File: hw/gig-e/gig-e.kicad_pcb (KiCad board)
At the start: 4 copper layers, 149 x 111.1 mm, 181 parts, among them U201 FDT434P, U202 KSZ9021GQ, U203 MIC5207-2.5YM5, U301 FDT434P, U302 KSZ9021GQ, U303 MIC5207-2.5YM5, X201 25MHz, X301 25MHz

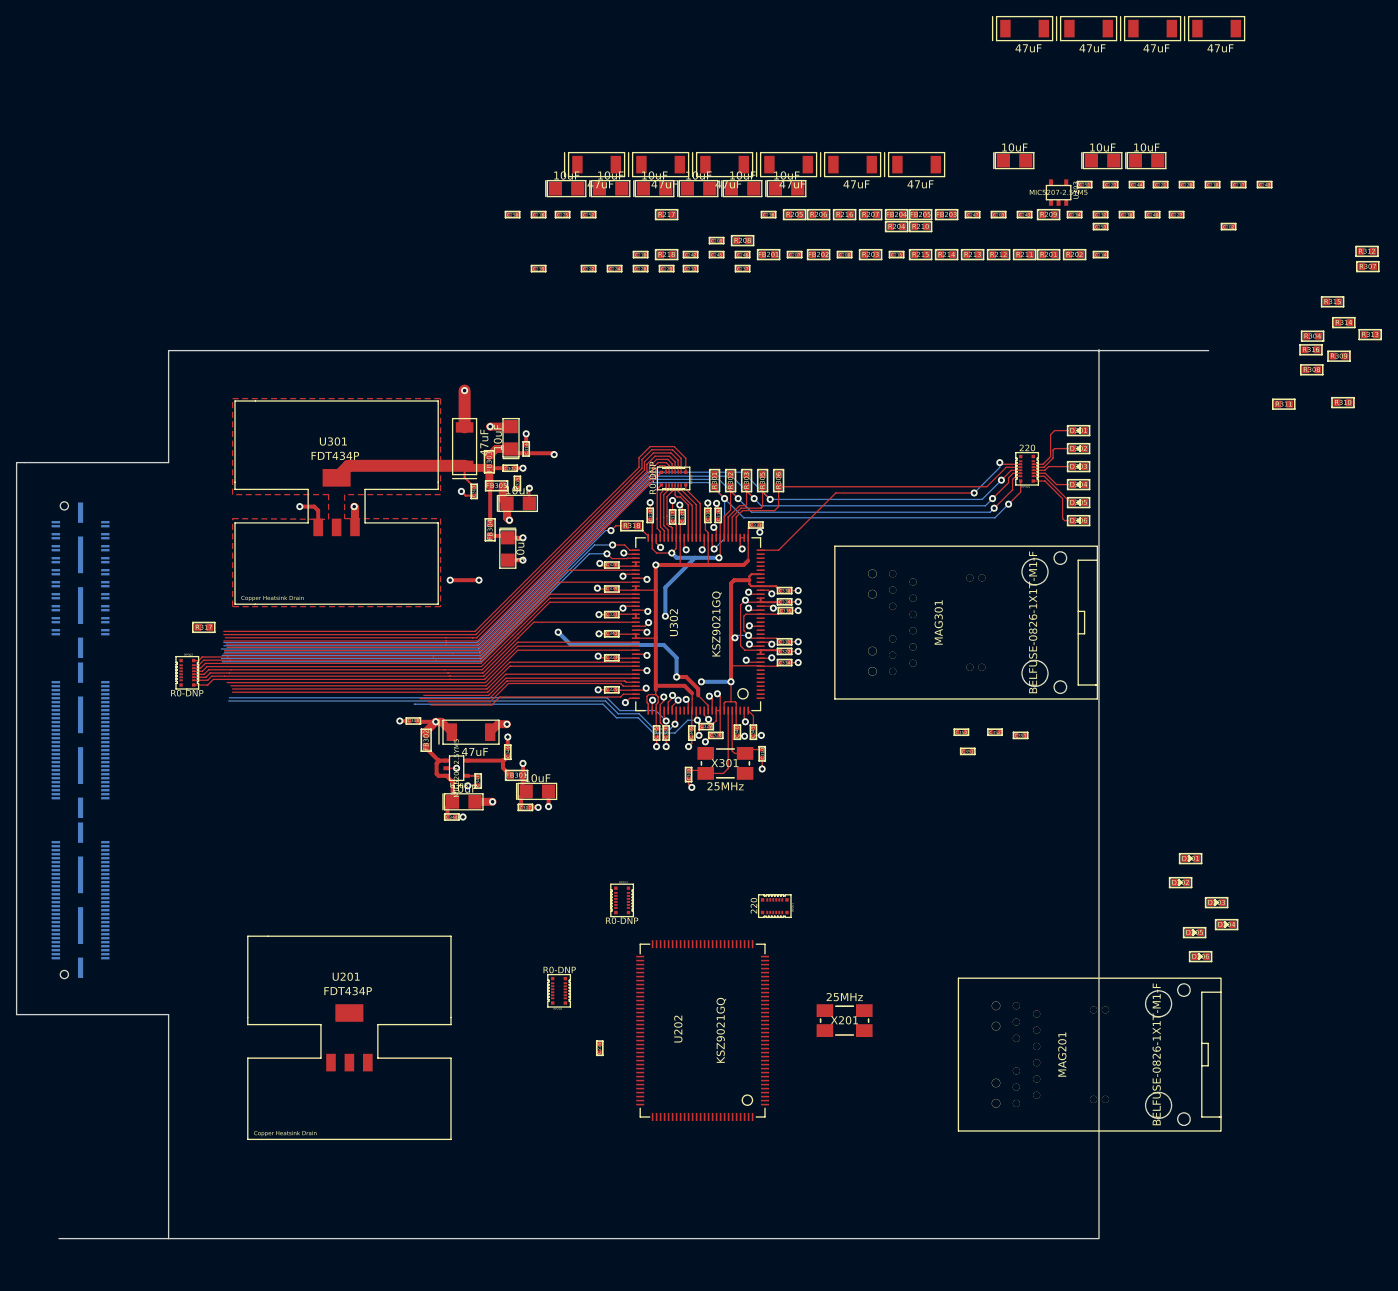
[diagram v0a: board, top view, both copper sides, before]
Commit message: gig-e board for DE2-115 completed
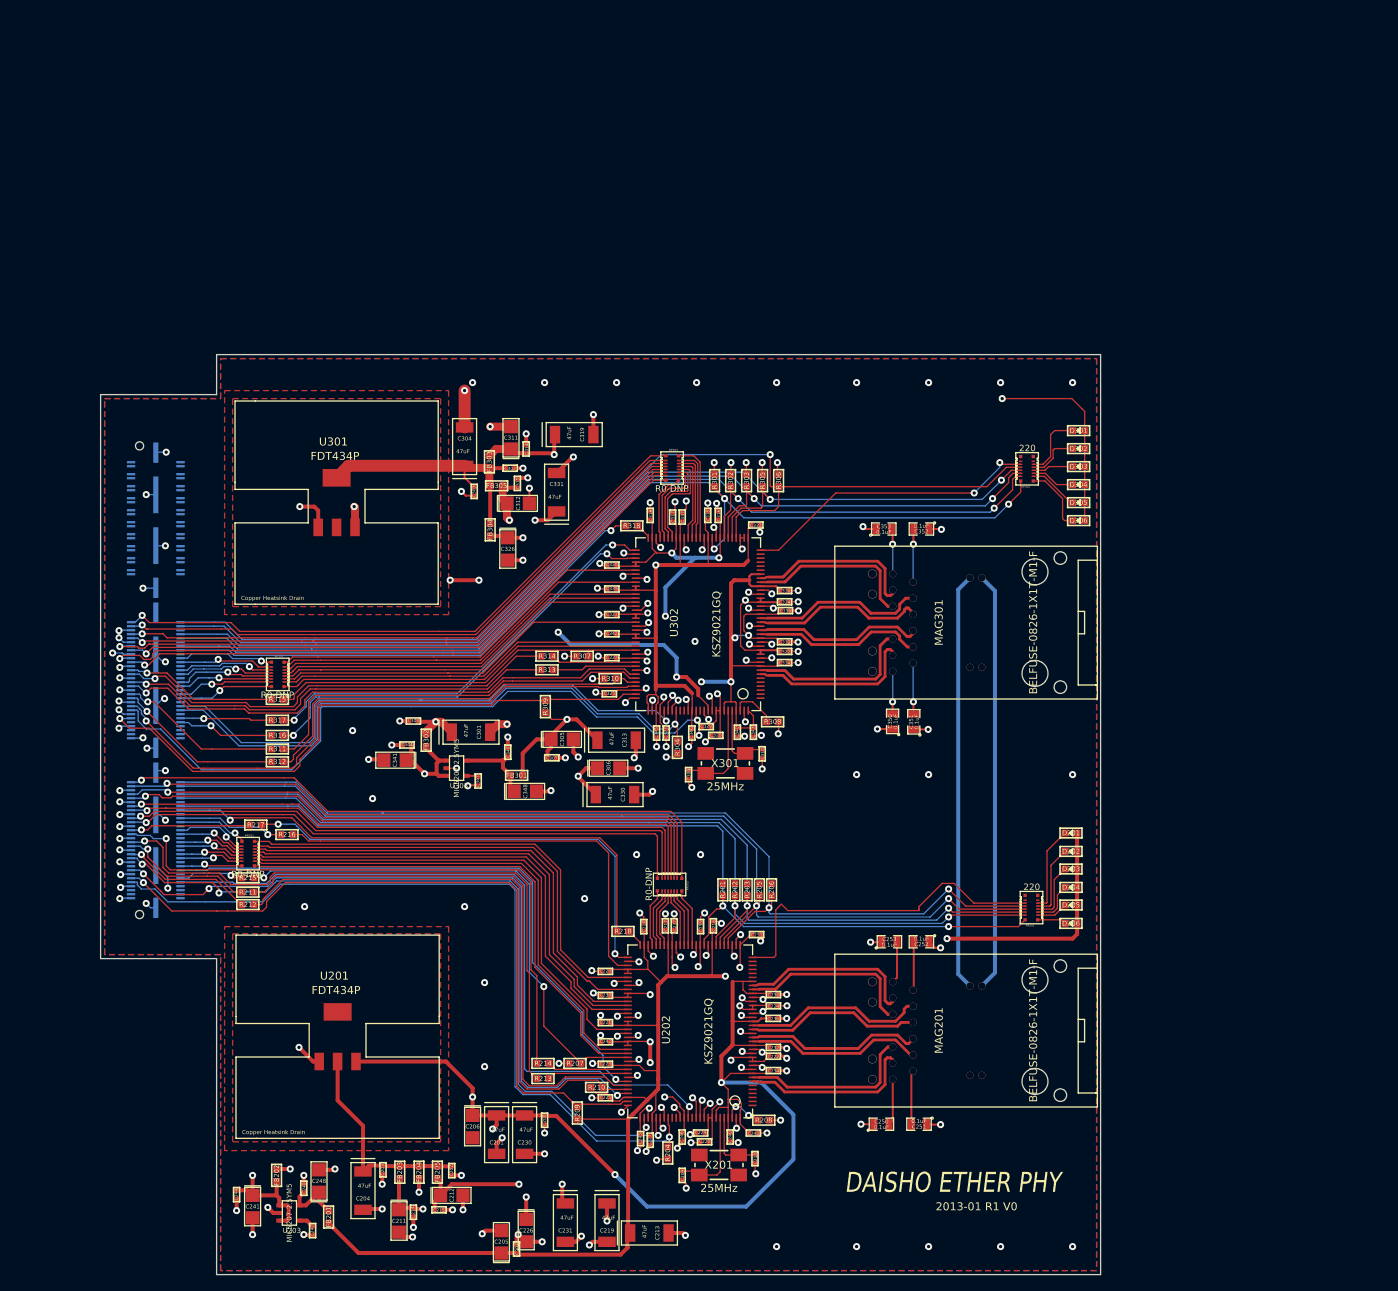
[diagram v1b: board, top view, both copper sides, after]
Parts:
- C250, C251, C252, C253, C350, C351, C352, C353: footprint GSG-0402 -> SM0805
- moved C249 173.7 mm to (114.9, 162.7), turned to 90 degrees
- moved C244 169.1 mm to (106.5, 163.5), turned to 270 degrees
- moved C213 166.4 mm to (158.1, 168.3)
- moved U203 159.7 mm to (113.1, 165.8), turned to 270 degrees
- moved C230 159.0 mm to (142.5, 156.0), turned to 270 degrees
- moved C212 155.8 mm to (133.4, 163.6)
- moved C202 152.8 mm to (133.4, 160.5), turned to 270 degrees
- moved C247 151.4 mm to (116.0, 168.0), turned to 270 degrees
- moved R312 150.4 mm to (111.6, 109.4), turned to 180 degrees
- moved C214 147.3 mm to (128.6, 165.7), turned to 270 degrees
- moved C204 142.1 mm to (122.3, 163.0), turned to 270 degrees
- moved C203 142.0 mm to (124.8, 160.4), turned to 270 degrees
- moved R315 141.0 mm to (111.6, 101.6), turned to 180 degrees
- moved R316 137.9 mm to (111.6, 106.1), turned to 180 degrees
- moved C211 137.8 mm to (126.8, 166.8), turned to 270 degrees
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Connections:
- JP101 pad 101: PHY0_GM_TXD7 -> PHY0_GM_TXD0
- JP101 pad 102: PHY1_GM_TXD7 -> PHY0_PHYADDR4
- JP101 pad 103: PHY0_GM_TXD6 -> PHY0_GM_TXD1
- JP101 pad 104: PHY1_GM_TXD6 -> PHY0_PHYADDR3
- JP101 pad 107: PHY0_GM_TXD5 -> PHY0_GM_TXD2
- JP101 pad 108: PHY1_GM_TXD5 -> PHY0_PHYADDR2
- JP101 pad 109: PHY0_GM_TXD4 -> PHY0_GM_TXD3
- JP101 pad 110: PHY1_GM_TXD4 -> PHY0_PHYADDR1
- JP101 pad 113: PHY0_GM_TXD3 -> PHY0_GM_TXD4
- JP101 pad 114: PHY1_GM_TXD3 -> PHY0_PHYADDR0
- JP101 pad 115: PHY0_GM_TXD2 -> PHY0_GM_TXD5
- JP101 pad 116: PHY1_GM_TXD2 -> PHY0_GM_TX_ER
- JP101 pad 119: PHY0_GM_TXD1 -> PHY0_GM_TXD6
- JP101 pad 120: PHY1_GM_TXD1 -> PHY0_GM_TX_EN
- JP101 pad 121: PHY0_GM_TXD0 -> PHY0_GM_TXD7
- JP101 pad 122: PHY1_GM_TXD0 -> PHY0_GM_RXD7
- JP101 pad 125: PHY0_PHYADDR1 -> PHY0_GM_GTK_CLK
- JP101 pad 126: PHY1_PHYADDR1 -> PHY0_GM_RXD6
- JP101 pad 127: PHY0_PHYADDR2 -> PHY0_GM_RX_ERR
- JP101 pad 128: PHY1_PHYADDR2 -> PHY0_GM_RXD5
- JP101 pad 131: PHY0_PHYADDR3 -> PHY0_GM_RX_CLK
- JP101 pad 132: PHY1_PHYADDR3 -> PHY0_GM_RXD4
- JP101 pad 133: PHY0_PHYADDR4 -> PHY0_GM_MDC
- JP101 pad 134: PHY1_PHYADDR4 -> PHY0_GM_RXD3
- JP101 pad 137: PHY0_RXDV -> PHY0_GM_MIO
- JP101 pad 138: PHY1_RXDV -> PHY0_GM_RXD2
- JP101 pad 139: PHY0_TX_CLK -> PHY0_CLK125_NDO
- JP101 pad 140: PHY1_TX_CLK -> PHY0_GM_RXD1
- JP101 pad 143: PHY0_HW_RST -> (no net)
- JP101 pad 144: PHY1_HW_RST -> PHY0_GM_RXD0
- JP101 pad 146: PHY1_COL -> PHY0_CRS
- JP101 pad 149: PHY1_CRS -> PHY0_INT_N
- JP101 pad 150: PHY1_CRS -> PHY0_GM_RXDV
- JP101 pad 151: (no net) -> PHY0_HW_RST
- JP101 pad 152: (no net) -> PHY0_TX_CLK
- JP101 pad 41: PHY0_GM_MDC -> PHY1_GM_TXD0
- JP101 pad 42: PHY1_GM_MDC -> PHY1_PHYADDR4
- JP101 pad 43: PHY0_GM_MIO -> PHY1_GM_TXD1
- JP101 pad 44: PHY1_GM_MIO -> PHY1_PHYADDR3
- JP101 pad 47: PHY0_GM_RX_CLK -> PHY1_GM_TXD2
- JP101 pad 48: PHY1_GM_RX_CLK -> PHY1_PHYADDR2
- JP101 pad 49: PHY0_GM_RX_ERR -> PHY1_GM_TXD3
- JP101 pad 50: PHY1_GM_RX_ERR -> PHY1_PHYADDR1
- JP101 pad 53: PHY0_GM_RXDV -> PHY1_GM_TXD4
- JP101 pad 54: PHY1_GM_RXDV -> PHY1_PHYADDR0
- JP101 pad 55: PHY0_GM_RXD7 -> PHY1_GM_TXD5
- JP101 pad 56: PHY1_GM_RXD7 -> PHY1_GM_TX_ER
- JP101 pad 59: PHY0_GM_RXD6 -> PHY1_GM_TXD6
- JP101 pad 60: PHY1_GM_RXD6 -> PHY1_GM_RXD7
- JP101 pad 61: PHY0_GM_RXD5 -> PHY1_GM_TXD7
- JP101 pad 62: PHY1_GM_RXD5 -> PHY1_GM_RXD6
- JP101 pad 65: PHY0_GM_RXD4 -> PHY1_GM_RXDV
- JP101 pad 66: PHY1_GM_RXD4 -> PHY1_GM_RXD5
- JP101 pad 67: PHY0_GM_RXD3 -> PHY1_GM_RX_ERR
- JP101 pad 68: PHY1_GM_RXD3 -> PHY1_GM_RXD4
- JP101 pad 71: PHY0_GM_RXD2 -> PHY1_GM_RX_CLK
- JP101 pad 72: PHY1_GM_RXD2 -> PHY1_GM_RXD3
- JP101 pad 73: PHY0_GM_RXD1 -> PHY1_CRS
- JP101 pad 74: PHY1_GM_RXD1 -> PHY1_GM_RXD2
- JP101 pad 77: PHY0_GM_RXD0 -> PHY1_GM_MDC
- JP101 pad 78: PHY1_GM_RXD0 -> PHY1_GM_RXD1
- JP101 pad 79: PHY0_GM_TX_EN -> PHY1_GM_MIO
- JP101 pad 80: PHY1_GM_TX_EN -> PHY1_GM_RXD0
- JP101 pad 83: PHY0_GM_GTK_CLK -> PHY1_COL
- JP101 pad 84: PHY1_GM_GTK_CLK -> PHY1_CLK125_NDO
- JP101 pad 85: PHY0_GM_TX_ER -> PHY1_TX_CLK
- JP101 pad 86: PHY1_GM_TX_ER -> PHY1_HW_RST
- JP101 pad 89: PHY0_CLK125_NDO -> PHY1_INT_N
- JP101 pad 90: PHY1_CLK125_NDO -> PHY1_GM_GTK_CLK
- JP101 pad 91: PHY0_PHYADDR0 -> (no net)
- JP101 pad 92: PHY1_PHYADDR0 -> PHY1_GM_TX_EN
- MAG201 pad 4: PHY0_TXRXP_B -> PHY0_TXRXM_B
- MAG201 pad 5: PHY0_TXRXM_B -> PHY0_TXRXP_B
- MAG201 pad 8: PHY0_TXRXP_D -> PHY0_TXRXM_D
- MAG201 pad 9: PHY0_TXRXM_D -> PHY0_TXRXP_D
- MAG301 pad 4: PHY1_TXRXP_B -> PHY1_TXRXM_B
- MAG301 pad 5: PHY1_TXRXM_B -> PHY1_TXRXP_B
- MAG301 pad 8: PHY1_TXRXP_D -> PHY1_TXRXM_D
- MAG301 pad 9: PHY1_TXRXM_D -> PHY1_TXRXP_D
- RP202 pad 1: /GigE Phy0/RXD7 -> /GigE Phy0/RXD0
- RP202 pad 10: PHY0_GM_RXD1 -> PHY0_GM_RXD6
- RP202 pad 11: PHY0_GM_RXD2 -> PHY0_GM_RXD5
- RP202 pad 12: PHY0_GM_RXD3 -> PHY0_GM_RXD4
- RP202 pad 13: PHY0_GM_RXD4 -> PHY0_GM_RXD3
- RP202 pad 14: PHY0_GM_RXD5 -> PHY0_GM_RXD2
- RP202 pad 15: PHY0_GM_RXD6 -> PHY0_GM_RXD1
- RP202 pad 16: PHY0_GM_RXD7 -> PHY0_GM_RXD0
- RP202 pad 2: /GigE Phy0/RXD6 -> /GigE Phy0/RXD1
- RP202 pad 3: /GigE Phy0/RXD5 -> /GigE Phy0/RXD2
- RP202 pad 4: /GigE Phy0/RXD4 -> /GigE Phy0/RXD3
- RP202 pad 5: /GigE Phy0/RXD3 -> /GigE Phy0/RXD4
- RP202 pad 6: /GigE Phy0/RXD2 -> /GigE Phy0/RXD5
- RP202 pad 7: /GigE Phy0/RXD1 -> /GigE Phy0/RXD6
- RP202 pad 8: /GigE Phy0/RXD0 -> /GigE Phy0/RXD7
- RP202 pad 9: PHY0_GM_RXD0 -> PHY0_GM_RXD7
- U202 pad 96: (no net) -> PHY0_CRS
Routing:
- net GND: track 109.2 -> 600.9 mm, vias 74 -> 219
- net /GigE Phy0/DVDDH: track 0.00 -> 200.9 mm, vias 0 -> 2
- net +3.3V: track 12.2 -> 184.2 mm, vias 0 -> 22
- net /GigE Phy0/AVDDH: track 0.00 -> 168.5 mm, vias 0 -> 5
- net PHY0_PHYADDR4: track 0.00 -> 127.9 mm, vias 0 -> 2
- net PHY0_PHYADDR3: track 0.00 -> 126.8 mm, vias 0 -> 2
- net PHY0_PHYADDR2: track 0.00 -> 125.9 mm, vias 0 -> 2
- net PHY0_PHYADDR1: track 0.00 -> 125.3 mm, vias 0 -> 2
- net PHY0_PHYADDR0: track 0.00 -> 125.1 mm, vias 0 -> 2
- net /GigE Phy0/DVDDL: track 0.00 -> 106.2 mm, vias 0 -> 10
- net PHY0_HW_RST: track 0.00 -> 101.1 mm, vias 0 -> 1
- net PHY0_CLK125_NDO: track 0.00 -> 98.5 mm, vias 0 -> 3
- net /GigE Phy1/DVDDH: track 86.3 -> 181.5 mm, vias 6 -> 10
- net /GigE Phy0/AVDDL: track 0.00 -> 94.6 mm, vias 0 -> 4
- net PHY0_INT_N: track 0.00 -> 91.9 mm, vias 0 -> 1
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- added copper zone on F.Cu, net /GigE Phy0/AVDDL_PMOS
- added copper zone on B.Cu, net GND
- added copper zone on F.Cu, net GND
- added copper zone on Inner1.Cu, net GND
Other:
- board size 149 x 111.1 mm -> 125 x 115 mm
- net class Default: via_drill 0.635 -> 0.4064
- rule pad_to_mask_clearance: 0 -> 0.1524
- board text added: "2013-01 R1 V0"
- board text added: "DAISHO ETHER PHY"

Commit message: hardware update including last minute gig-e corrections
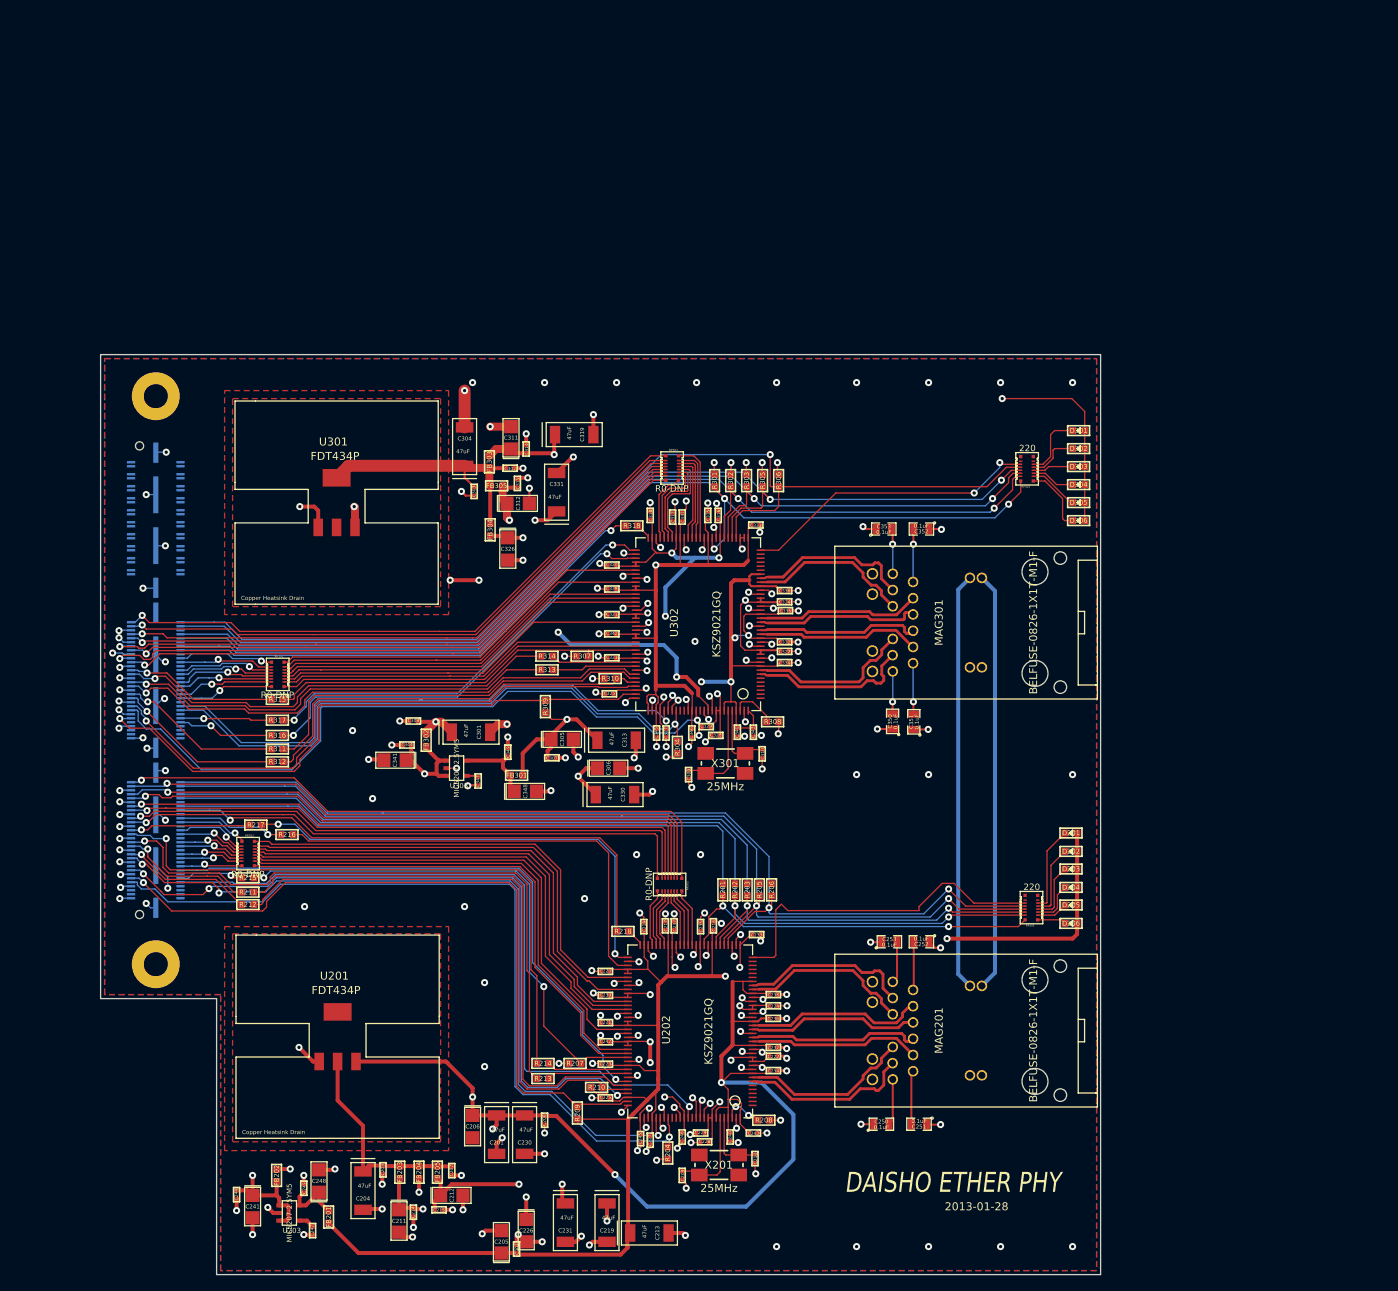
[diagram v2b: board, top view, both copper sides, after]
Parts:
- JP101: footprint TERASIC-HSMC -> TERASIC-HSMC-WITH-MOUNTS
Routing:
- net PHY1_TXRXM_C: track 21.6 -> 20.4 mm
- net PHY1_TXRXP_C: track 21.6 -> 20.4 mm
- net PHY1_TXRXM_D: track 21.5 -> 20.4 mm
- net PHY1_TXRXP_D: track 21.5 -> 20.4 mm
- net PHY0_TXRXM_D: track 22.4 -> 21.4 mm
- net PHY0_TXRXP_D: track 22.4 -> 21.4 mm
- net PHY1_TXRXP_B: track 21.3 -> 20.4 mm
- net PHY1_TXRXM_B: track 21.3 -> 20.5 mm
- net PHY0_TXRXM_A: track 22.2 -> 21.4 mm
- net PHY0_TXRXP_A: track 22.2 -> 21.4 mm
- net PHY1_TXRXM_A: track 21.2 -> 20.4 mm
- net PHY0_TXRXP_B: track 22.2 -> 21.4 mm
- net PHY1_TXRXP_A: track 21.2 -> 20.5 mm
- net PHY0_TXRXM_B: track 22.1 -> 21.5 mm
- net +3.3V: track 184.2 -> 183.5 mm
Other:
- outline, holes or cut-outs redrawn
- board text added: "2013-01-28"
- board text removed: "2013-01 R1 V0"

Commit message: gig-e updates
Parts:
- moved C232 1.00 mm to (174.6, 145.2)
- moved C222 1.00 mm to (174.6, 146.2)
- moved C225 1.00 mm to (151.6, 151.4)
- moved C224 0.86 mm to (174.4, 140.1)
- moved RP201 0.81 mm to (205.1, 127.2)
- moved C234 0.80 mm to (174.4, 148.1)
- moved C238 0.70 mm to (174.3, 138.6)
- moved C328 0.69 mm to (166.8, 106.7), turned to 0 degrees
- moved C329 0.63 mm to (165.4, 105.6)
- moved C327 0.55 mm to (160.2, 106.3)
- moved C316 0.54 mm to (166.5, 78.1)
- moved C335 0.50 mm to (165.3, 78.1)
- moved C242 0.47 mm to (153.0, 144.7)
- moved C336 0.45 mm to (175.6, 90.5)
- moved RP202 0.45 mm to (108.2, 120.5)
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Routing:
- net GND: track 600.9 -> 619.9 mm
- net /GigE Phy0/AVDDH: track 168.2 -> 170.1 mm
- net /GigE Phy0/AVDDL: track 94.6 -> 95.9 mm
- net /GigE Phy1/AVDD_PLL: track 48.9 -> 49.9 mm
- net PHY0_PHYADDR2: track 125.9 -> 124.9 mm
- net PHY0_PHYADDR4: track 127.9 -> 126.9 mm
- net PHY1_CLK125_NDO: track 71.6 -> 72.6 mm
- net /GigE Phy0/LED6: track 43.2 -> 42.3 mm
- net PHY0_PHYADDR1: track 125.3 -> 124.4 mm
- net /GigE Phy0/LED1_D: track 3.59 -> 4.42 mm
- net PHY0_INT_N: track 91.9 -> 92.7 mm
- net /GigE Phy1/DVDDL: track 102.6 -> 103.4 mm
- net /GigE Phy0/LED2_D: track 3.92 -> 4.66 mm
- net /GigE Phy1/AVDDH: track 161.7 -> 162.4 mm
- net /GigE Phy0/TXD0: track 7.30 -> 6.67 mm
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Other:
- board text added: "2013-02-04"
- board text added: "MAG201"
- board text added: "MAG301"
- board text added: "PHY0"
- board text added: "PHY1"
- board text removed: "2013-01-28"
